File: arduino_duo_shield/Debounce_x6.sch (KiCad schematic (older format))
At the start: 23 parts, among them U3 74HC14, U6 74HC14

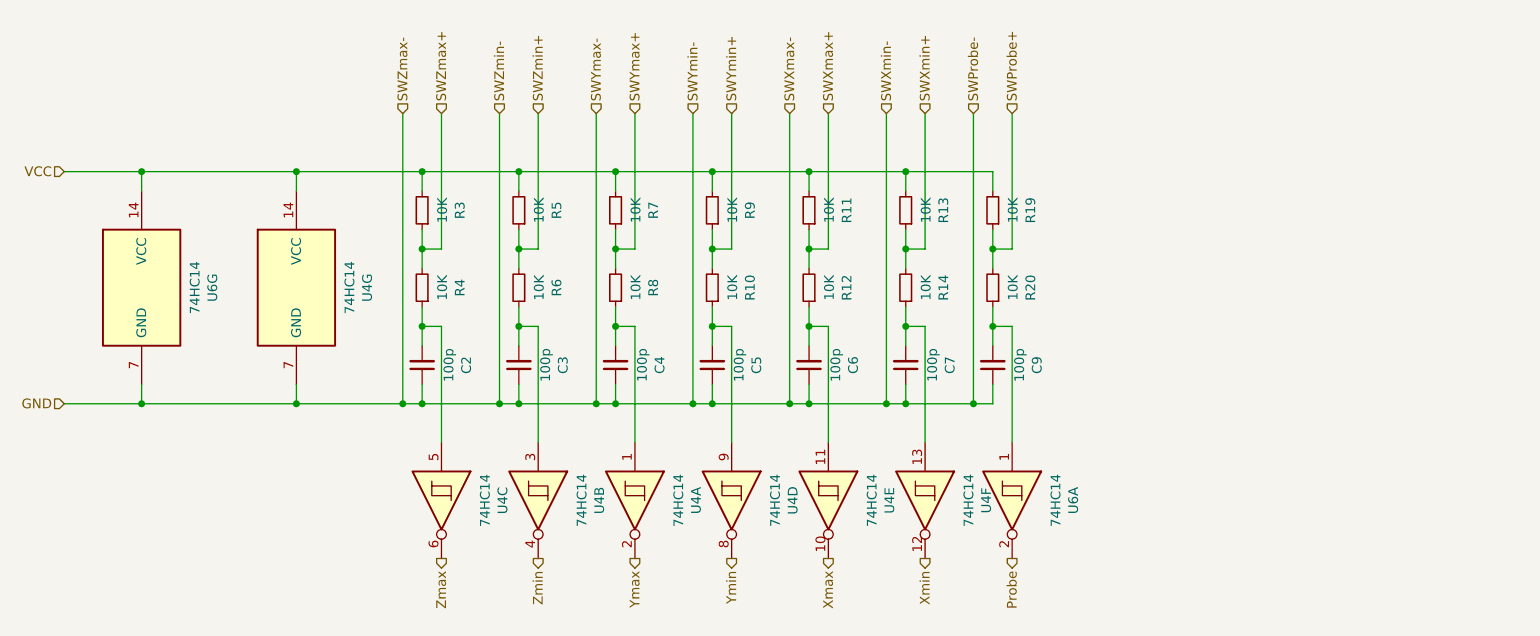
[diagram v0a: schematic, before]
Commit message: Add signal mirror and control jumpers
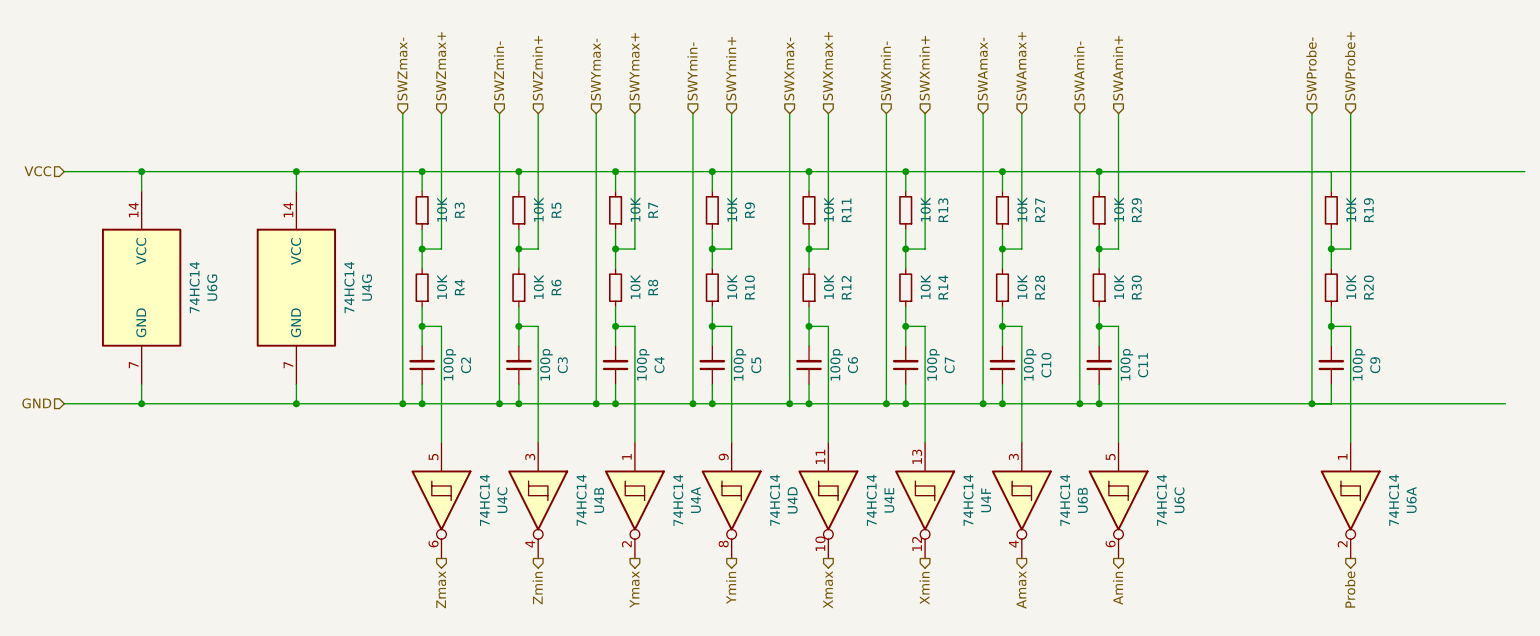
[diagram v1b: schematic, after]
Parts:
- added C10, C11: 100p, Capacitor_THT:C_Disc_D3.0mm_W2.0mm_P2.50mm, symbol Device:C_Small
- added R27, R28, R29, R30: 10K, Resistor_THT:R_Axial_DIN0207_L6.3mm_D2.5mm_P7.62mm_Horizontal, symbol Device:R_Small
- added unit 2 of U6
- added unit 3 of U6
- R1, R10, R11, R12, R19, R2, R20, R3, R4, R5, R6, R7, R8, R9: footprint Resistor_THT:R_Axial_DIN0204_L3.6mm_D1.6mm_P5.08mm_Horizontal -> Resistor_THT:R_Axial_DIN0207_L6.3mm_D2.5mm_P7.62mm_Horizontal
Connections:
- net GND: now also C10.1, C11.1
- net VCC: now also R27.2, R29.2
- new net: C11.2, R30.1, U6.5
- new net: C10.2, R28.1, U6.3
- new net Amax: U6.4
- new net Amin: U6.6
- new net SWAmax+: R27.1, R28.2
- new net SWAmin+: R29.1, R30.2
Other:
- moved on the sheet: C9, R19, R20, U6A
